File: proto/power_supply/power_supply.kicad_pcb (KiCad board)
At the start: 2 copper layers, 100 x 100 mm, 98 parts, among them J101 Conn_01x02, J102 Conn_01x02, J103 Conn_01x02, J301 Conn_01x04, J302 Conn_01x08, J303 Conn_ARM_JTAG_SWD_20, Q201 BC846, SW301 SW_Push_Dual, U101 ZXCT1110, U102 ZXCT1110, U103 LDK130-33_SOT23_SOT353, U201 TPS61178, U202 TSV911xxLx, U301 STM32G051C6Tx, U401 TSV914, U409 TSV914

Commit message: Finish alim sch, start PCB
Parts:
- removed the C104 at (96.0, 61.5)
- removed C411, C413: 100n, Capacitor_SMD:C_0805_2012Metric
- removed C412, C415, C416: 100p, Capacitor_SMD:C_0805_2012Metric
- removed the R103 at (94.5, 74.2)
- removed R104: 6.8k, Resistor_SMD:R_0805_2012Metric
- removed R202: 1Meg, Resistor_SMD:R_0805_2012Metric
- removed R207: 10k, Resistor_SMD:R_0805_2012Metric
- removed RV202: 200k (0k), Potentiometer_THT:Potentiometer_Bourns_3296W_Vertical
- removed TP105: V_{IIN}, TestPoint:TestPoint_Keystone_5010-5014_Multipurpose
- removed TP106: V_{IOUT}, TestPoint:TestPoint_Keystone_5010-5014_Multipurpose
- removed the U102 at (157.2, 74.2)
- removed U409: TSV914, Package_SO:SOIC-14_3.9x8.7mm_P1.27mm
- added C101: 47u, Capacitor_THT:CP_Radial_D5.0mm_P2.50mm, F.Cu at (87.5, 50.2)
- added C401: 100p, Capacitor_SMD:C_0805_2012Metric, F.Cu at (232.6, 73.5)
- added C402: 100p, Capacitor_SMD:C_0805_2012Metric, F.Cu at (232.6, 76.5)
- added C407: 100p, Capacitor_SMD:C_0805_2012Metric, F.Cu at (237.0, 82.5)
- added C408: 100p, Capacitor_SMD:C_0805_2012Metric, F.Cu at (237.0, 85.5)
- added C409: 100n, Capacitor_SMD:C_0805_2012Metric, F.Cu at (237.0, 73.5)
- added D201: XBS104S14R-G, Diode_SMD:D_SOD-123, F.Cu at (143.1, 87.5)
- added Q202: TK4R3E06PL, Package_TO_SOT_THT:TO-220-3_Horizontal_TabUp, F.Cu at (135.5, 65.2)
- added Q203: BC846, Package_TO_SOT_SMD:SOT-23, F.Cu at (252.4, 102.6)
- added R204: 12k, Resistor_SMD:R_0805_2012Metric, F.Cu at (239.7, 136.7)
- added R211: 1k8, Resistor_SMD:R_0805_2012Metric, F.Cu at (148.5, 75.0)
- added R212: 200k, Resistor_SMD:R_0805_2012Metric, F.Cu at (237.6, 115.1)
- added R213: 10k, Resistor_SMD:R_0805_2012Metric, F.Cu at (237.6, 118.1)
- added R214: 150k, Resistor_SMD:R_0805_2012Metric, F.Cu at (143.5, 71.0)
- added R215: 15k, Resistor_SMD:R_0805_2012Metric, F.Cu at (141.0, 71.0)
- added TP204: V_{FB}, TestPoint:TestPoint_Keystone_5010-5014_Multipurpose, F.Cu at (232.9, 108.6)
- added U203: TSV911xxLx, Package_TO_SOT_SMD:SOT-23-5, F.Cu at (252.5, 98.2)
- added U402: TSV914, Package_SO:SOIC-14_3.9x8.7mm_P1.27mm, F.Cu at (243.5, 88.9)
- C201, C202, C203, C206, C207, C208: value 15u -> 47u; footprint Capacitor_SMD:C_0805_2012Metric -> Capacitor_SMD:C_1206_3216Metric
- C204: value 100n -> 47u; footprint Capacitor_SMD:C_0805_2012Metric -> Capacitor_SMD:C_1206_3216Metric
- C205: value 1u -> 47u; footprint Capacitor_SMD:C_0805_2012Metric -> Capacitor_SMD:C_1206_3216Metric
- C209: value 470p -> 47u; footprint Capacitor_SMD:C_0805_2012Metric -> Capacitor_SMD:C_1206_3216Metric
- C210: value 100n -> 100n/16V
- C211: value 100n -> 1u
- C212: value NM -> 47n
- C213, C214, C215: value NM -> 100n
- C410: value 100p -> 100n
- L201: value 1u5 -> 22u; footprint power_supply:SRP0620 -> Inductor_SMD:L_Coilcraft_XAL1510-223
- Q201: value BC846 -> TK4R3E06PL; footprint Package_TO_SOT_SMD:SOT-23 -> Package_TO_SOT_THT:TO-220-3_Horizontal_TabUp
- R101: value 10m -> 8m; footprint Resistor_SMD:R_1206_3216Metric -> Resistor_SMD:R_2512_6332Metric
- R102: value 10m -> 12k; footprint Resistor_SMD:R_1206_3216Metric -> Resistor_SMD:R_0805_2012Metric
- R201: value 1Meg -> 8m; footprint Resistor_SMD:R_0805_2012Metric -> Resistor_SMD:R_2512_6332Metric
- R203: value 12k -> 2
- R205: value 220k -> 2
- R206: value 68k -> 2
- R208: value 1k8 -> 470k
- R209: value 200k -> 12k
- RV201: value 200k (80k) -> 200k (0k)
- TP103: value TestPoint -> V_{IIN}
- TP104: value TestPoint -> V_{IOUT}
- TP201: value V_{BJT} -> TestPoint
- TP202: value R_{ILIMIT} -> TestPoint
- TP203: value V_{CTRL} -> V_{SW}
- TP205: value V_{FB} -> V_{CTRL}
- TP206: value V_{SW} -> V_{BJT}
- U201: value TPS61178 -> ZXCT1110; footprint power_supply:VSON-TPS61178 -> Package_TO_SOT_SMD:SOT-23-5
- U202: value TSV911xxLx -> TPS43060; footprint Package_TO_SOT_SMD:SOT-23-5 -> power_supply:QFN-16_EP_3x3_Pitch0.5mm
- moved TP101 180.8 mm to (261.2, 98.5)
- moved U101 177.4 mm to (266.3, 104.7), turned to 0 degrees
- moved TP102 169.6 mm to (261.2, 103.5)
- moved R405 157.8 mm to (245.9, 73.4), turned to 0 degrees
- moved R407 157.6 mm to (245.9, 79.3)
- moved TP202 156.8 mm to (240.0, 157.5)
- moved R402 153.8 mm to (241.5, 76.4)
- moved R401 153.6 mm to (241.5, 73.4), turned to 0 degrees
- moved R415 153.5 mm to (254.7, 79.3), turned to 0 degrees
- moved R409 151.3 mm to (250.3, 73.4), turned to 0 degrees
- moved R412 147.0 mm to (250.3, 82.3), turned to 0 degrees
- moved R411 146.9 mm to (250.3, 79.3)
- moved C403 144.5 mm to (232.6, 79.5)
- moved C405 144.5 mm to (232.6, 85.5)
- moved RV201 140.9 mm to (253.6, 114.2)
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- renumbered C101 to C102, C102 to C103, C103 to C104, R105 to R103, U103 to U102
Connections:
- C203 pad 1: /Vin -> /Vout
- C204 pad 1: /Core/BST -> /Vout
- C204 pad 2: /Core/SW -> GND
- C205 pad 1: /Core/u1_VCC -> /Vout
- C209 pad 1: Net-(U201-COMP) -> /Vout
- C209 pad 2: Net-(C209-Pad2) -> GND
- C210 pad 1: Net-(U202-+) -> /Core/BST
- C210 pad 2: GND -> /Core/SW
- C211 pad 1: +3.3V -> /Core/DRIVER_VCC
- C212 pad 1: Net-(U201-COMP) -> Net-(U202-COMP)
- C212 pad 2: Net-(C209-Pad2) -> Net-(C212-Pad2)
- C213 pad 1: Net-(U201-COMP) -> Net-(U203-+)
- C213 pad 2: Net-(C209-Pad2) -> GND
- C214 pad 1: Net-(U201-COMP) -> +3.3V
- C214 pad 2: Net-(C209-Pad2) -> GND
- C215 pad 1: Net-(U201-COMP) -> Net-(U202-SS)
- C215 pad 2: Net-(C209-Pad2) -> GND
- C403 pad 1: Net-(C403-Pad1) -> Net-(U401C-+)
- C403 pad 2: /Analog Interface/Iin_filtered -> GND
- C404 pad 1: Net-(C404-Pad1) -> Net-(U402D-+)
- C404 pad 2: /Analog Interface/Iout_filtered -> GND
- C405 pad 1: Net-(U409C-+) -> Net-(C405-Pad1)
- C405 pad 2: GND -> /Analog Interface/Vin_filtered
- C406 pad 1: Net-(U401D-+) -> Net-(C406-Pad1)
- C406 pad 2: GND -> /Analog Interface/Vout_filtered
- C410 pad 1: Net-(C410-Pad1) -> GND
- C410 pad 2: /Analog Interface/Vin_filtered -> +3.3V
- J101 pad 1: /Vin_raw -> /Vin
- L201 pad 1: /Vin -> /Core/DRV_VIN
- Q201 pad 1: Net-(Q201-B) -> Net-(Q201-G)
- Q201 pad 2: GND -> /Vout
- Q201 pad 3: /Core/FB -> /Core/SW
- R101 pad 1: /Vin_raw -> /Output
- R101 pad 2: /Vin -> /Vout
- R102 pad 1: /Vout -> /Iout
- R102 pad 2: /Output -> GND
- R201 pad 1: GND -> /Core/DRV_VIN
- R201 pad 2: /Core/BST -> /Vin
- R203 pad 1: /Core/FB -> Net-(Q201-G)
- R203 pad 2: /Vout -> Net-(U202-HDRV)
- R205 pad 1: Net-(U201-FREQ) -> /Core/DRIVER_VCC
- R205 pad 2: GND -> Net-(U202-EN)
- R206 pad 1: Net-(C209-Pad2) -> Net-(U202-LDRV)
- R206 pad 2: GND -> Net-(Q202-G)
- R208 pad 1: GND -> Net-(U202-RT)
- R208 pad 2: /Core/FB -> GND
- R209 pad 1: Net-(U202--) -> /Core/FB
- R209 pad 2: Net-(R209-Pad2) -> /Vout
- R210 pad 1: Net-(U202-+) -> /AlimCTRL
- R210 pad 2: GND -> Net-(U203-+)
- R401 pad 2: Net-(C403-Pad1) -> Net-(C401-Pad1)
- R402 pad 1: Net-(C403-Pad1) -> Net-(C401-Pad1)
- R402 pad 2: Net-(U409C-+) -> Net-(U401C-+)
- R403 pad 2: Net-(C404-Pad1) -> Net-(C402-Pad1)
- R404 pad 1: Net-(C404-Pad1) -> Net-(C402-Pad1)
- R404 pad 2: Net-(U401D-+) -> Net-(U402D-+)
- R405 pad 1: Net-(U409B--) -> Net-(U401B--)
- R406 pad 1: Net-(U401A--) -> Net-(U402A--)
- R407 pad 2: Net-(U409B--) -> Net-(U401B--)
- R408 pad 2: Net-(U401A--) -> Net-(U402A--)
- R409 pad 2: Net-(U409A-+) -> Net-(U401A-+)
- R410 pad 2: Net-(U401B-+) -> Net-(U402B-+)
- R411 pad 2: Net-(C410-Pad1) -> Net-(C405-Pad1)
- R412 pad 1: Net-(C410-Pad1) -> Net-(C405-Pad1)
- R412 pad 2: Net-(U409D-+) -> Net-(U401D-+)
- R413 pad 2: Net-(C412-Pad1) -> Net-(C406-Pad1)
- R414 pad 1: Net-(C412-Pad1) -> Net-(C406-Pad1)
- R414 pad 2: Net-(U401C-+) -> Net-(U402C-+)
- R415 pad 1: Net-(U409A-+) -> Net-(U401A-+)
- R416 pad 1: Net-(U401B-+) -> Net-(U402B-+)
- RV201 pad 1: Net-(U201-ILIMIT) -> Net-(Q203-B)
- RV201 pad 2: Net-(U201-ILIMIT) -> Net-(R212-Pad2)
- RV201 pad 3: GND -> Net-(R212-Pad2)
- TP101 pad 1: /Vin_raw -> /Vout
- TP102 pad 1: /Vin -> /Output
- TP103 pad 1: /Vout -> /Analog Interface/Iin
- TP104 pad 1: /Output -> /Iout
- TP201 pad 1: Net-(Q201-B) -> /Vin
- TP202 pad 1: Net-(U201-ILIMIT) -> /Core/DRV_VIN
- TP203 pad 1: Net-(U202-+) -> /Core/SW
- TP205 pad 1: /Core/FB -> Net-(U203-+)
- TP206 pad 1: /Core/SW -> Net-(Q203-B)
- TP207 pad 1: Net-(U202--) -> Net-(U203--)
- U101 pad 3: /Analog Interface/Iin -> /Iout
- U101 pad 4: /Vin_raw -> /Vout
- U101 pad 5: /Vin -> /Output
- U201 pad 1: Net-(U201-FREQ) -> unconnected-(U201-NC-Pad1)
- U201 pad 3: Net-(U201-ILIMIT) -> /Analog Interface/Iin
- U201 pad 4: Net-(U201-COMP) -> /Vin
- U201 pad 5: /Core/FB -> /Core/DRV_VIN
- U202 pad 1: Net-(U202--) -> Net-(U202-RT)
- U202 pad 2: GND -> Net-(U202-SS)
- U202 pad 3: Net-(U202-+) -> Net-(U202-COMP)
- U202 pad 4: Net-(U202--) -> /Core/FB
- U202 pad 5: +3.3V -> /Core/DRV_VIN
- U401 pad 1: /Analog Interface/Iout_MEAS -> /Analog Interface/Vin_MEAS
- U401 pad 13: /Analog Interface/Iout_filtered -> /Analog Interface/Vin_filtered
- U401 pad 14: /Analog Interface/Iout_filtered -> /Analog Interface/Vin_filtered
- U401 pad 2: Net-(U401A--) -> /Analog Interface/Vin_MEAS
- U401 pad 3: /Iout -> Net-(U401A-+)
- U401 pad 5: Net-(U401B-+) -> /Analog Interface/Iin
- U401 pad 6: /Analog Interface/Vout_MEAS -> Net-(U401B--)
- U401 pad 7: /Analog Interface/Vout_MEAS -> /Analog Interface/Iin_MEAS
- U401 pad 8: /Analog Interface/Vout_filtered -> /Analog Interface/Iin_filtered
- U401 pad 9: /Analog Interface/Vout_filtered -> /Analog Interface/Iin_filtered
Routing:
- net +3.3V: track 230.5 -> 120.7 mm, vias 9 -> 6
- net /Analog Interface/Iout_filtered: track 95.1 -> 0.00 mm, vias 2 -> 0
- net /Analog Interface/Iout_MEAS: track 94.4 -> 0.00 mm, vias 2 -> 0
- net /Analog Interface/Vout_MEAS: track 89.6 -> 0.00 mm, vias 2 -> 0
- net /Analog Interface/Vout_filtered: track 82.4 -> 0.00 mm, vias 2 -> 0
- net /Analog Interface/Iin_MEAS: track 54.9 -> 0.00 mm, vias 2 -> 0
- net /Analog Interface/Vin_MEAS: track 54.6 -> 0.00 mm, vias 2 -> 0
- net /Analog Interface/Iin_filtered: track 49.7 -> 0.00 mm, vias 2 -> 0
- net /Vin_raw: track 44.5 -> 0.00 mm
- net /Analog Interface/Vin_filtered: track 42.4 -> 0.00 mm, vias 2 -> 0
- net /Vin: track 41.0 -> 0.00 mm, vias 2 -> 0
- net /AlimCTRL: track 38.5 -> 0.00 mm, vias 2 -> 0
- net /Vout: track 41.4 -> 5.69 mm, vias 0 -> 1
- net /Core/FB: track 32.5 -> 2.18 mm, vias 2 -> 0
- net /Output: track 30.2 -> 0.00 mm, vias 0 -> 6
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- added copper zone on F.Cu, net /Core/DRV_VIN
- added copper zone on B.Cu, net /Output
- removed copper zone on F.Cu, net /Vin_raw
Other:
- board text added: "Air flow"
- board text removed: "Analog section"

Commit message: Update PCB
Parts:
- moved R415 163.2 mm to (91.5, 76.5), turned to 90 degrees
- moved U401 160.5 mm to (91.5, 87.6), turned to -90 degrees
- moved R402 159.6 mm to (82.5, 90.5), turned to -90 degrees
- moved R405 159.5 mm to (86.5, 80.5), turned to 90 degrees
- moved R401 157.6 mm to (84.0, 80.5), turned to -90 degrees
- moved R407 156.9 mm to (89.0, 80.5), turned to -90 degrees
- moved R409 156.3 mm to (94.0, 76.5), turned to -90 degrees
- moved C403 153.0 mm to (80.0, 90.5), turned to 90 degrees
- moved R411 152.0 mm to (98.5, 86.5), turned to -90 degrees
- moved U201 150.9 mm to (100.5, 75.5), turned to 90 degrees
- moved R412 149.5 mm to (101.0, 90.6), turned to -90 degrees
- moved R204 149.3 mm to (101.5, 80.0), turned to -90 degrees
- moved C401 148.6 mm to (85.0, 90.5), turned to -90 degrees
- moved C410 144.6 mm to (92.5, 81.5), turned to 180 degrees
- moved U203 134.6 mm to (118.5, 86.0)
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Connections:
- U202 pad 7: /Core/DRV_VIN -> /Vin
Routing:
- net /Vin: track 0.00 -> 155.4 mm, vias 0 -> 6
- net /Core/DRV_VIN: track 0.00 -> 89.7 mm, vias 0 -> 4
- net /Analog Interface/Iin_MEAS: track 0.00 -> 61.7 mm, vias 0 -> 2
- net /Analog Interface/Iin_filtered: track 0.00 -> 61.4 mm, vias 0 -> 2
- net /Analog Interface/Vin_MEAS: track 0.00 -> 49.7 mm, vias 0 -> 2
- net /Analog Interface/Vin_filtered: track 0.00 -> 48.8 mm, vias 0 -> 2
- net /Core/FB: track 2.18 -> 42.0 mm
- net /AlimCTRL: track 0.00 -> 30.7 mm
- net /Analog Interface/Iin: track 0.00 -> 23.1 mm
- net Net-(U401D-+): track 0.00 -> 14.8 mm
- net Net-(U401C-+): track 0.00 -> 14.3 mm
- net Net-(C401-Pad1): track 0.00 -> 11.1 mm
- net Net-(U203--): track 0.00 -> 10.5 mm
- net Net-(U401A-+): track 0.00 -> 10.4 mm
- net +3.3V: track 120.7 -> 110.9 mm, vias 6 -> 2
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
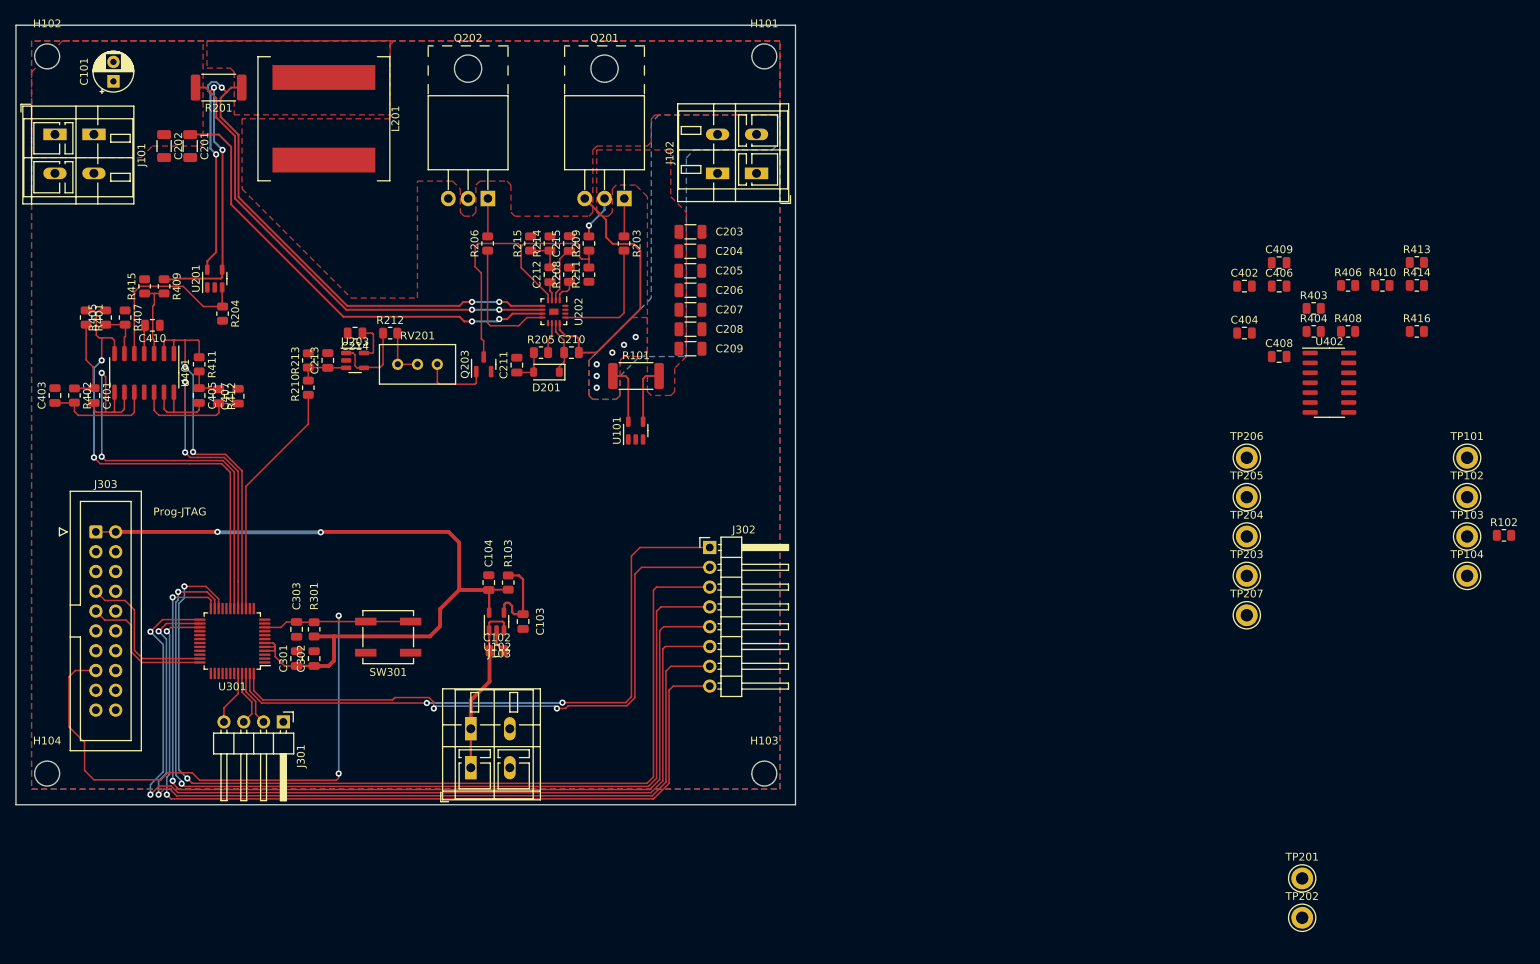
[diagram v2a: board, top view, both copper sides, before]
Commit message: Finish first routing
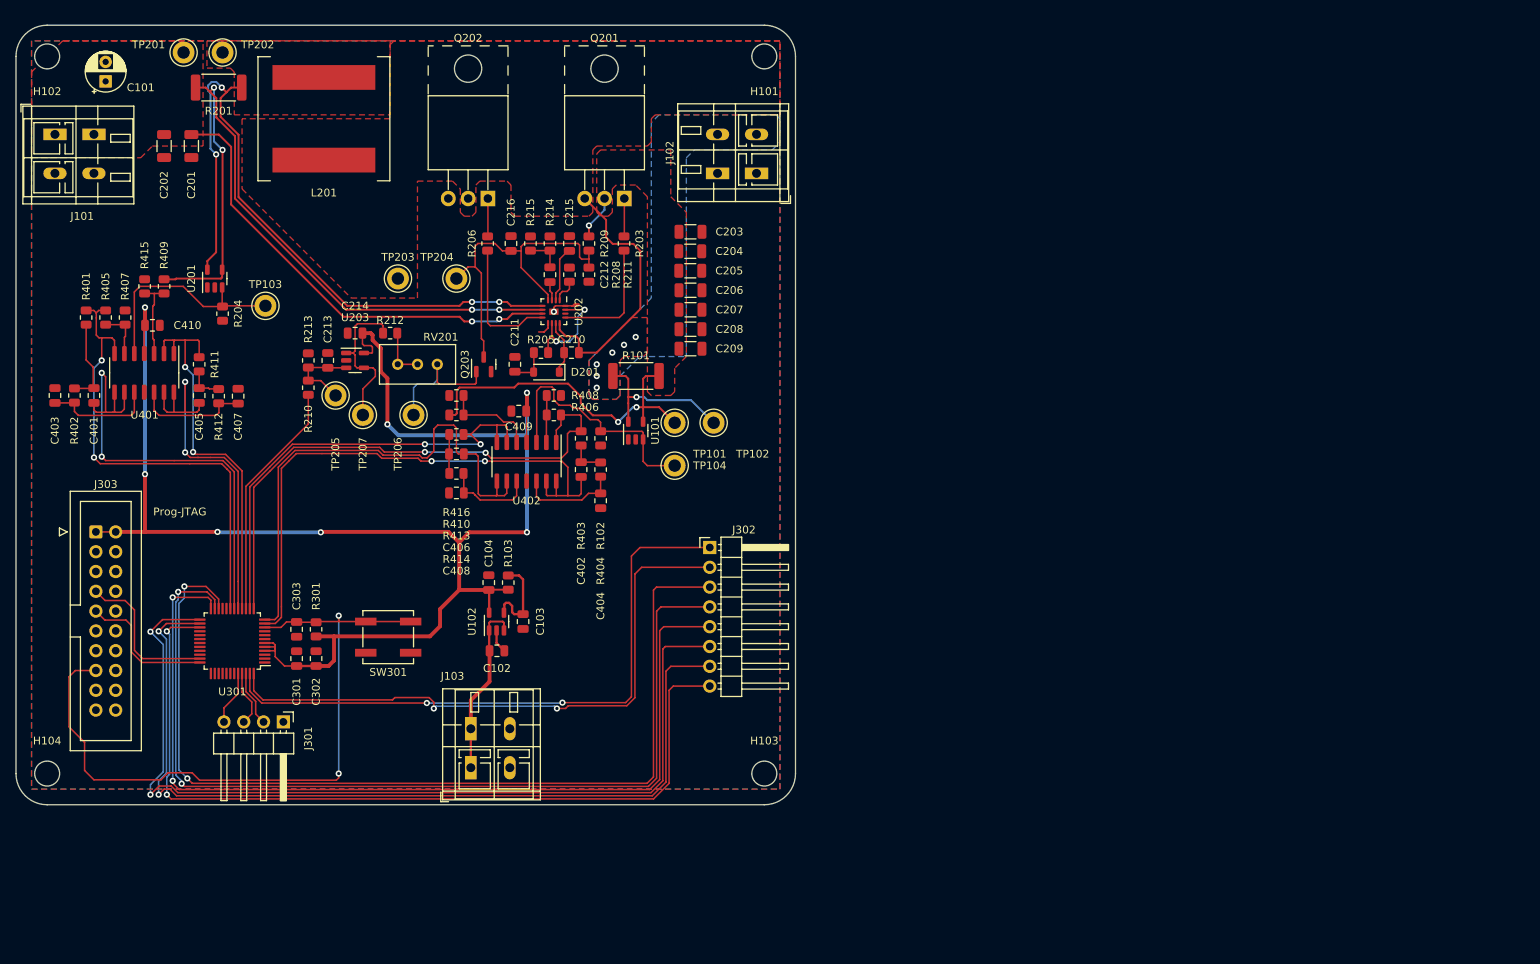
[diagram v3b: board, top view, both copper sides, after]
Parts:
- added C216: 15p, Capacitor_SMD:C_0805_2012Metric, F.Cu at (138.5, 71.0)
- moved TP201 178.4 mm to (96.5, 46.5)
- moved TP202 177.5 mm to (101.5, 46.5)
- moved TP103 157.0 mm to (107.0, 79.0)
- moved R414 125.5 mm to (131.5, 100.5)
- moved R413 125.2 mm to (131.5, 95.5), turned to 180 degrees
- moved R416 123.5 mm to (131.5, 90.5), turned to 180 degrees
- moved R410 120.0 mm to (131.5, 93.0)
- moved TP205 117.6 mm to (116.0, 90.5)
- moved R102 116.6 mm to (150.0, 96.0), turned to -90 degrees
- moved TP207 116.3 mm to (119.5, 93.0)
- moved TP203 115.4 mm to (124.0, 75.5)
- moved C406 107.7 mm to (131.5, 98.0)
- moved TP206 107.0 mm to (126.0, 93.0)
- moved C408 107.0 mm to (131.5, 103.0), turned to 180 degrees
- moved TP204 106.7 mm to (131.5, 75.5)
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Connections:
- U202 pad 17: (no net) -> GND
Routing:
- net +3.3V: track 110.9 -> 207.1 mm, vias 2 -> 7
- net /Analog Interface/Iout_filtered: track 0.00 -> 73.9 mm, vias 0 -> 2
- net /Analog Interface/Iout_MEAS: track 0.00 -> 71.4 mm, vias 0 -> 2
- net /Analog Interface/Vout_filtered: track 0.00 -> 67.0 mm
- net /Analog Interface/Vout_MEAS: track 0.00 -> 59.7 mm, vias 0 -> 2
- net /Vout: track 13.4 -> 49.9 mm, vias 1 -> 3
- net /Iout: track 0.00 -> 32.4 mm
- net Net-(U402D-+): track 0.00 -> 12.9 mm
- net /Output: track 7.63 -> 19.9 mm, vias 6 -> 7
- net Net-(U402B-+): track 0.00 -> 12.1 mm
- net Net-(U402C-+): track 0.00 -> 11.8 mm
- net Net-(U202-EN): track 3.98 -> 13.9 mm, vias 0 -> 2
- net Net-(U203--): track 10.5 -> 20.2 mm
- net Net-(Q203-B): track 8.93 -> 17.4 mm
- net GND: track 3.03 -> 10.3 mm, vias 0 -> 1
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- added copper zone on In1.Cu, net GND
- added copper zone on In2.Cu, net GND
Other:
- outline, holes or cut-outs redrawn
- copper layers 2 -> 4

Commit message: Update planes and fix DRC
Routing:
- net GND: track 10.3 -> 68.9 mm, vias 1 -> 24
- net /Output: track 19.9 -> 21.7 mm, vias 7 -> 8
- net Net-(U202-HDRV): track 15.8 -> 14.6 mm
- net /Vout: track 49.9 -> 50.6 mm
- net /Core/SW: track 34.4 -> 33.9 mm
- added copper zone on B.Cu, net /Core/SW
- added copper zone on B.Cu, net /Vout

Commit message: Improve overall
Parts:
- added C304: C, Capacitor_SMD:C_0805_2012Metric, F.Cu at (114.0, 118.0)
- added C305: C, Capacitor_SMD:C_0805_2012Metric, F.Cu at (116.5, 118.0)
- added J304: Conn_01x03, Connector_PinHeader_2.54mm:PinHeader_1x03_P2.54mm_Horizontal, F.Cu at (102.5, 132.5)
- added R302: 0, Resistor_SMD:R_0805_2012Metric, F.Cu at (111.5, 118.0)
- added TP105: TestPoint, TestPoint:TestPoint_Keystone_5010-5014_Multipurpose, F.Cu at (132.5, 124.0)
- added TP106: TestPoint, TestPoint:TestPoint_Keystone_5010-5014_Multipurpose, F.Cu at (132.5, 119.0)
- added TP107: TestPoint, TestPoint:TestPoint_Keystone_5010-5014_Multipurpose, F.Cu at (163.5, 138.0)
- added Y301: 8MHz, Crystal:Crystal_SMD_5032-2Pin_5.0x3.2mm, F.Cu at (114.0, 114.0)
- moved C303 12.8 mm to (119.0, 110.5), turned to 90 degrees
- moved R301 12.7 mm to (121.5, 110.6), turned to -90 degrees
- moved J301 4.74 mm to (114.0, 132.5)
- moved SW301 1.75 mm to (124.5, 121.5)
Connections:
- U301 pad 29: unconnected-(U301-PA9/NC-Pad29) -> Net-(J304-Pin_3)
- U301 pad 32: unconnected-(U301-PA10/NC-Pad32) -> Net-(J304-Pin_2)
- U301 pad 8: unconnected-(U301-PF0-Pad8) -> Net-(U301-PF0)
- U301 pad 9: unconnected-(U301-PF1-Pad9) -> Net-(U301-PF1)
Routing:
- net /Control/~{RST}: track 91.2 -> 109.5 mm
- net Net-(U301-PF0): track 0.00 -> 17.9 mm
- net Net-(J304-Pin_3): track 0.00 -> 13.9 mm, vias 0 -> 1
- net Net-(J304-Pin_2): track 0.00 -> 13.2 mm, vias 0 -> 1
- net Net-(C304-Pad1): track 0.00 -> 6.98 mm
- net Net-(U301-PF1): track 0.00 -> 5.35 mm
- net +3.3V: track 207.1 -> 212.3 mm
- net /Control/I2C_SDA: track 7.15 -> 12.1 mm
- net Net-(J103-Pin_1): track 22.6 -> 26.3 mm
- net /Control/I2C_SCL: track 7.16 -> 9.81 mm
- net GND: track 68.9 -> 71.1 mm
- net /Vout: track 50.6 -> 51.2 mm
- net /Control/I2C_SMBA: track 6.97 -> 7.55 mm

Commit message: Update with additional PSU from output
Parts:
- added C105: 100n, Capacitor_SMD:C_0805_2012Metric, F.Cu at (148.8, 110.0)
- added C106: 10u, Capacitor_SMD:C_0805_2012Metric, F.Cu at (147.0, 123.0)
- added C107: 10u, Capacitor_SMD:C_0805_2012Metric, F.Cu at (144.5, 123.0)
- added JP101: SolderJumper_3_Open, Jumper:SolderJumper-3_P2.0mm_Open_TrianglePad1.0x1.5mm, F.Cu at (140.5, 124.0)
- added JP102: EN DIG SUPPLY, Jumper:SolderJumper-2_P1.3mm_Open_TrianglePad1.0x1.5mm, F.Cu at (156.0, 104.2)
- added JP103: LINK_GND, Jumper:SolderJumper-2_P1.3mm_Open_TrianglePad1.0x1.5mm, F.Cu at (142.3, 118.5)
- added L101: 3.3u, Inductor_SMD:L_6.3x6.3_H3, F.Cu at (150.0, 117.0)
- added R104: 22k, Resistor_SMD:R_0805_2012Metric, F.Cu at (155.0, 119.0)
- added R105: 3.3k, Resistor_SMD:R_0805_2012Metric, F.Cu at (155.0, 115.0)
- added R106: 10k, Resistor_SMD:R_0805_2012Metric, F.Cu at (152.5, 104.0)
- added U103: LMR51430, Package_TO_SOT_SMD:SOT-23-6, F.Cu at (153.0, 110.0)
- moved TP106 7.43 mm to (127.0, 114.0)
- moved TP107 5.83 mm to (166.5, 133.0)
- moved TP105 4.52 mm to (132.1, 119.5)
- moved C102 2.21 mm to (134.5, 123.0), turned to 180 degrees
- moved C103 1.60 mm to (139.5, 118.0)
- moved U102 1.51 mm to (136.5, 118.0)
- moved C104 1.01 mm to (135.5, 113.5)
- moved R103 1.01 mm to (138.0, 113.5)
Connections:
- C102 pad 1: Net-(J103-Pin_1) -> Net-(JP101-C)
- TP105 pad 1: Net-(J103-Pin_1) -> Net-(JP101-C)
- U102 pad 1: Net-(J103-Pin_1) -> Net-(JP101-C)
- U102 pad 3: Net-(J103-Pin_1) -> Net-(JP101-C)
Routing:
- net /Output: track 21.7 -> 53.5 mm
- net Net-(JP101-B): track 0.00 -> 19.8 mm
- net Net-(JP101-C): track 0.00 -> 17.2 mm
- net Net-(U103-FB): track 0.00 -> 16.6 mm, vias 0 -> 2
- net Net-(U103-SW): track 0.00 -> 8.40 mm
- net Net-(J103-Pin_1): track 26.3 -> 18.4 mm
- net Net-(JP102-A): track 0.00 -> 7.67 mm
- net Net-(U103-BOOT): track 0.00 -> 5.72 mm
- net Net-(J302-Pin_1): track 80.7 -> 78.4 mm
- net Net-(J302-Pin_2): track 79.4 -> 77.2 mm
- net GND: track 71.1 -> 73.0 mm, vias 24 -> 57
- net Net-(J302-Pin_3): track 123.4 -> 121.9 mm
- net Net-(U102-BP): track 11.2 -> 9.93 mm
- net Net-(J302-Pin_4): track 121.3 -> 120.1 mm
- net +3.3V: track 212.3 -> 213.3 mm
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
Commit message: Document PCB
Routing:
- net /Control/~{RST}: track 109.5 -> 115.3 mm
- net /Vout: track 51.2 -> 50.5 mm
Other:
- board text added: "+3V3"
- board text added: "5V"
- board text added: "DRVIN"
- board text added: "EN PSU"
- board text added: "FB"
- board text added: "FBCTRL 1"
- board text added: "FBCTRL 2"
- board text added: "FBCTRL 3"
- board text added: "GND"
- board text added: "GPIO"
- board text added: "I2C"
- board text added: "INPUT PWR Vin GND"
- board text added: "Iin"
- board text added: "Iout"
- board text added: "LINK GND"
- board text added: "LOGIC PWR +5V GND"
- board text added: "OUTPUT 16V GND"
- board text added: "Output"
- board text added: "PB10"
- board text added: "PB11"
- board text added: "PB12"
- board text added: "PB13"
- board text added: "PB14"
- board text added: "PB15"
- board text added: "PB8"
- board text added: "PB9"
- board text added: "RESET"
- board text added: "RX"
- board text added: "SCL"
- board text added: "SDA"
- board text added: "SMBA"
- board text added: "SW"
- board text added: "TX"
- board text added: "UART1"
- board text added: "Vin"
- board text added: "Vout"
